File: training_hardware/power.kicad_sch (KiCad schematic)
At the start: 3 parts, among them U2 OKI

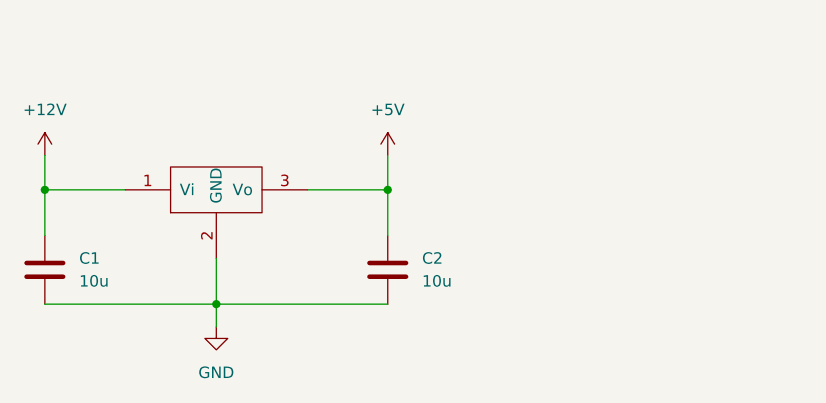
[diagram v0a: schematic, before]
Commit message: add ethernet
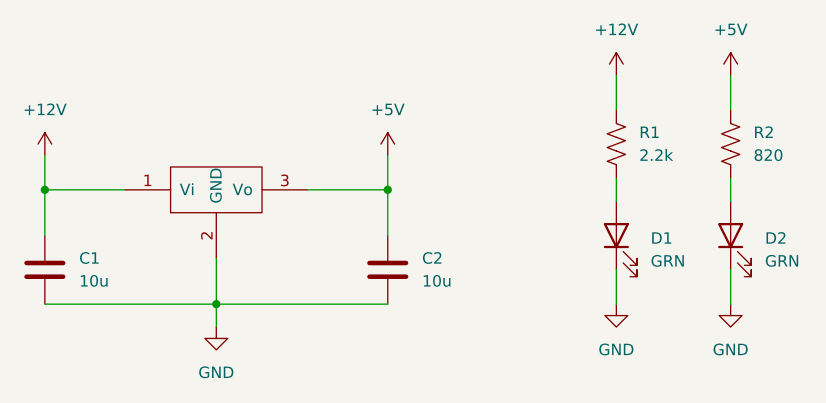
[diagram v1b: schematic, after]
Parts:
- added D1, D2: GRN, symbol Device:LED
- added R1: 2.2k, symbol Device:R_US
- added R2: 820, symbol Device:R_US
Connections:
- net +12V: now also R1.1
- net +5V: now also R2.1
- net GND: now also D1.1 (K), D2.1 (K)
- new net: D2.2 (A), R2.2
- new net: D1.2 (A), R1.2
